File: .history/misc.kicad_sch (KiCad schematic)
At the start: 7 parts, among them J3 Connector

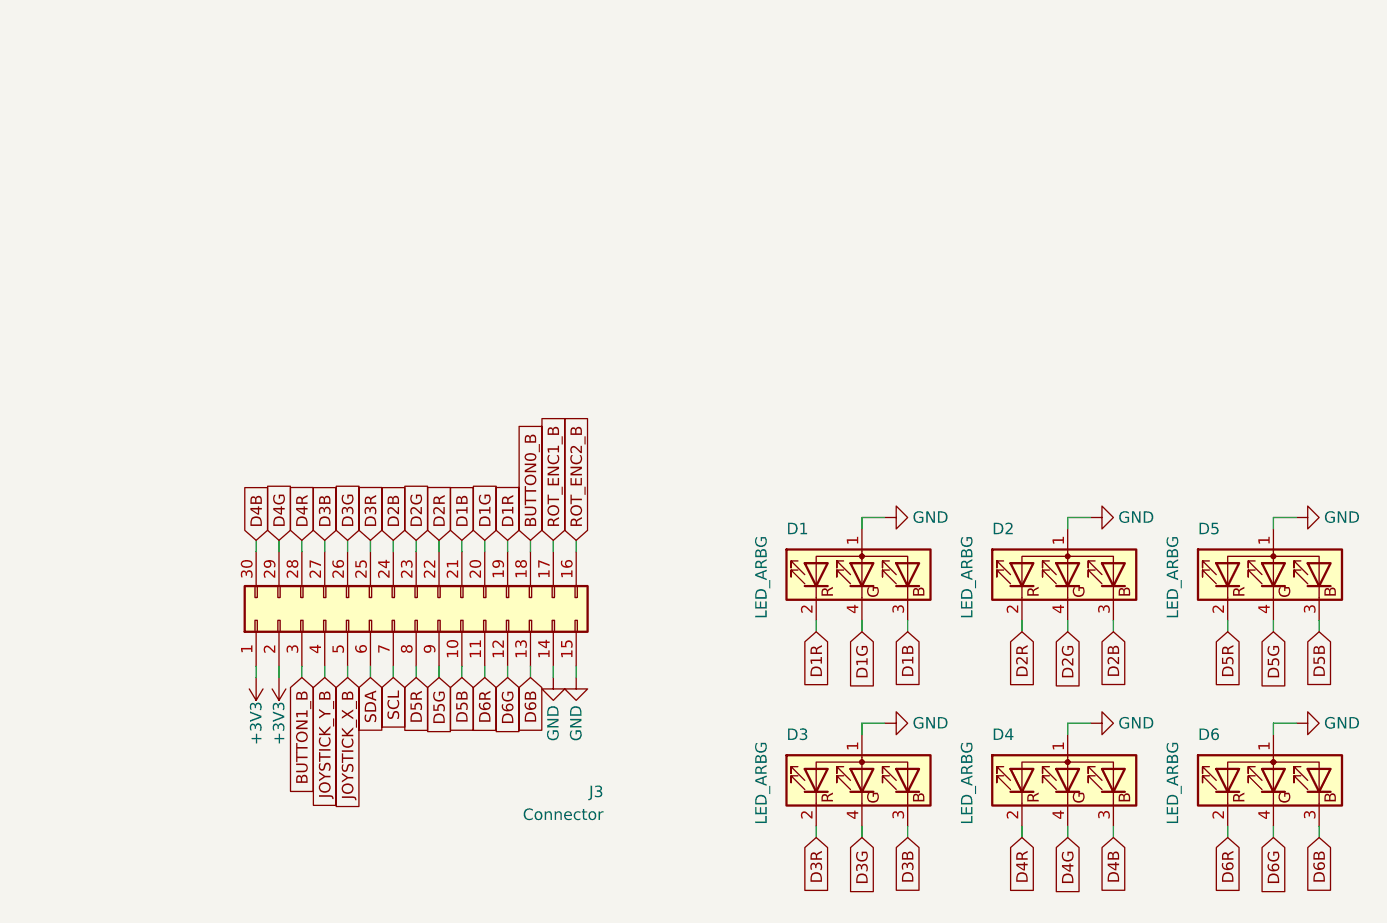
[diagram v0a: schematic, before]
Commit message: Routed secondary PCB with Power and charging managment, and routed FPC Connector
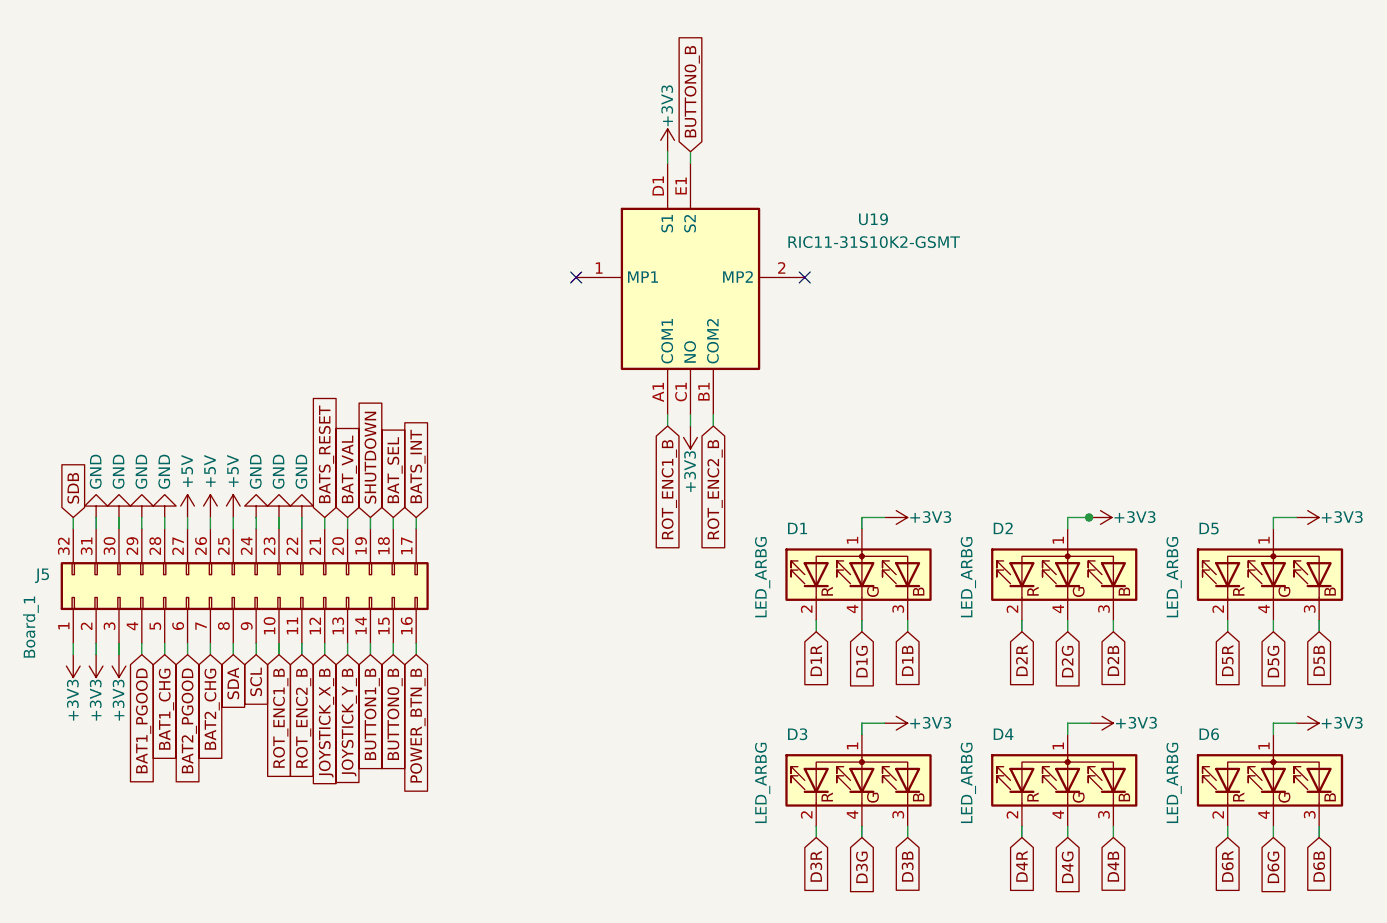
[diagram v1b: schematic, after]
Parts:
- removed J3: Connector, Connector_FFC-FPC:Amphenol_F32R-1A7x1-11029_1x29-1MP_P0.5mm_Horizontal, symbol Connector_Generic:Conn_02x15_Counter_Clockwise
- added J5: Board_1, Connector_FFC-FPC:Molex_502244-3330_1x33-1MP_P0.5mm_Horizontal, symbol Connector_Generic:Conn_02x16_Counter_Clockwise
- added U19: RIC11-31S10K2-GSMT, PTCR:RIC1131S10K2GSMT, symbol PTCR-V5:RIC11-31S10K2-GSMT
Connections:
- net +3V3: now also D1.1 (A), D2.1 (A), D3.1 (A), D4.1 (A), D5.1 (A), D6.1 (A), J5.1 (Pin_1), J5.2 (Pin_2), J5.3 (Pin_3), U19.C1 (NO), U19.D1 (S1)
- net BUTTON0_B: now also J5.15 (Pin_15), U19.E1 (S2)
- net BUTTON1_B: now also J5.14 (Pin_14)
- net GND: now also J5.22 (Pin_22), J5.23 (Pin_23), J5.24 (Pin_24), J5.28 (Pin_28), J5.29 (Pin_29), J5.30 (Pin_30), J5.31 (Pin_31); no longer D1.1 (A), D2.1 (A), D3.1 (A), D4.1 (A), D5.1 (A), D6.1 (A)
- net JOYSTICK_X_B: now also J5.12 (Pin_12)
- net JOYSTICK_Y_B: now also J5.13 (Pin_13)
- net ROT_ENC1_B: now also J5.10 (Pin_10), U19.A1 (COM1)
- net ROT_ENC2_B: now also J5.11 (Pin_11), U19.B1 (COM2)
- net SCL: now also J5.9 (Pin_9)
- net SDA: now also J5.8 (Pin_8)
- new net +5V: J5.25 (Pin_25), J5.26 (Pin_26), J5.27 (Pin_27)
- new net BAT1_CHG: J5.5 (Pin_5)
- new net BAT1_PGOOD: J5.4 (Pin_4)
- new net BAT2_CHG: J5.7 (Pin_7)
- new net BAT2_PGOOD: J5.6 (Pin_6)
- new net BATS_INT: J5.17 (Pin_17)
- new net BATS_RESET: J5.21 (Pin_21)
- new net BAT_SEL: J5.18 (Pin_18)
- new net BAT_VAL: J5.20 (Pin_20)
- new net POWER_BTN_B: J5.16 (Pin_16)
- new net SDB: J5.32 (Pin_32)
- new net SHUTDOWN: J5.19 (Pin_19)
- no-connect marks 0 -> 2
